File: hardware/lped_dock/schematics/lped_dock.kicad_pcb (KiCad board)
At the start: 2 copper layers, 35.4 x 16 mm, 25 parts, among them J2 V_{OUT}, J3 BUTTON, J4 CONN, J5 LED, J6 GND, J7 USB-C connector, SW1 Pair button, U1 TPD4E02B04DQA, U2 TPS560200

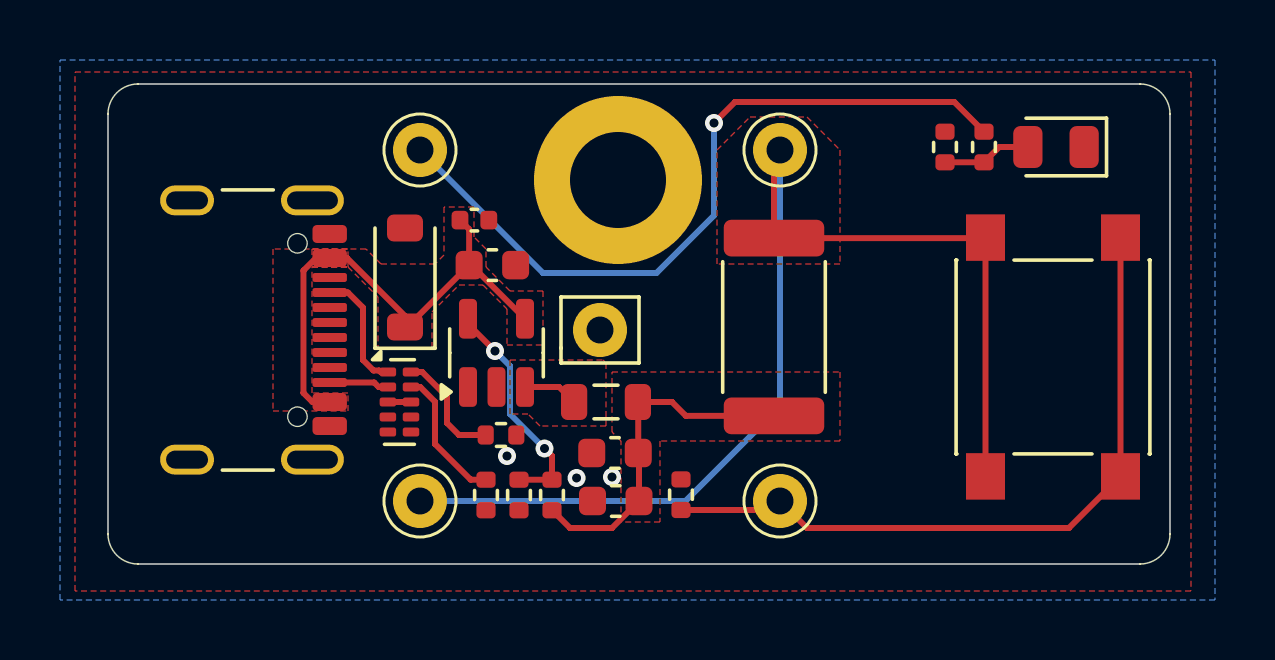
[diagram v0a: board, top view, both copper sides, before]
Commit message: feat(hardware): remove unused parts from dock pcb
* Removed LED from dock
* Removed button from dock
* Removed connection pins for LED and button
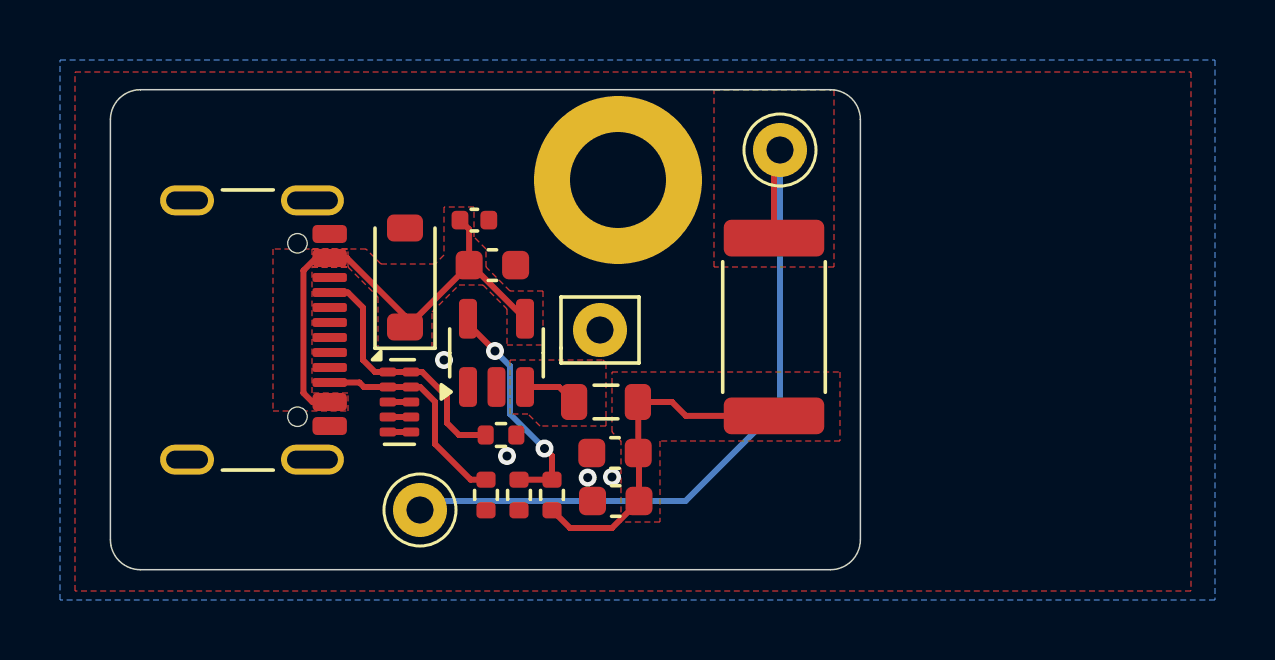
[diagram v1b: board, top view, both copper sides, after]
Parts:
- removed D1: LED, Diode_SMD:D_0805_2012Metric
- removed the J3 at (125.0, 112.7)
- removed J5: LED, Connector_Pin:Pin_D0.9mm_L10.0mm_W2.4mm_FlatFork
- removed R1: 1k, Resistor_SMD:R_0402_1005Metric
- removed R7, R8: 10k, Resistor_SMD:R_0402_1005Metric
- removed SW1: Pair button, Button_Switch_SMD:SW_SPST_PTS645
- moved J2 0.30 mm to (113.0, 113.0)
- renumbered J2 to J1, J4 to J2, J6 to J3
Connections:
- J7 pad A5: /USB/USB_CC1 -> /USB/CC1
- J7 pad B5: /USB/USB_CC2 -> /USB/CC2
- U1 pad 1: /USB/USB_CC1 -> /USB/CC1
- U1 pad 2: /USB/USB_CC2 -> /USB/CC2
- U1 pad 4: /USB/USB_D- -> /USB/D-
- U1 pad 5: /USB/USB_D+ -> /USB/D+
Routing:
- net /Dice Connector/LED: track 25.1 -> 0.00 mm, vias 1 -> 0
- net /Dice Connector/BUTTON: track 23.8 -> 0.00 mm
- net 3V6: track 39.9 -> 24.9 mm
- net /USB/CC1: track 3.87 -> 8.70 mm
- net /USB/USB_CC1: track 4.06 -> 0.00 mm
- net Net-(D1-A): track 2.97 -> 0.00 mm
- net /USB/CC2: track 4.60 -> 7.38 mm
- net /USB/USB_CC2: track 2.00 -> 0.00 mm
- net /USB/D-: track 0.00 -> 0.77 mm
- net /USB/D+: track 0.00 -> 0.77 mm
- net Earth: vias 3 -> 4
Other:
- board size 35.4 x 16 mm -> 25 x 16 mm
- board text added: "V2.0"
- board text removed: "BUTTON"
- board text removed: "LED"
- board text removed: "V1.0"

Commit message: feat(hardware): minor single dock improvements
* Moved connection pins closer together
* Added ground stiching
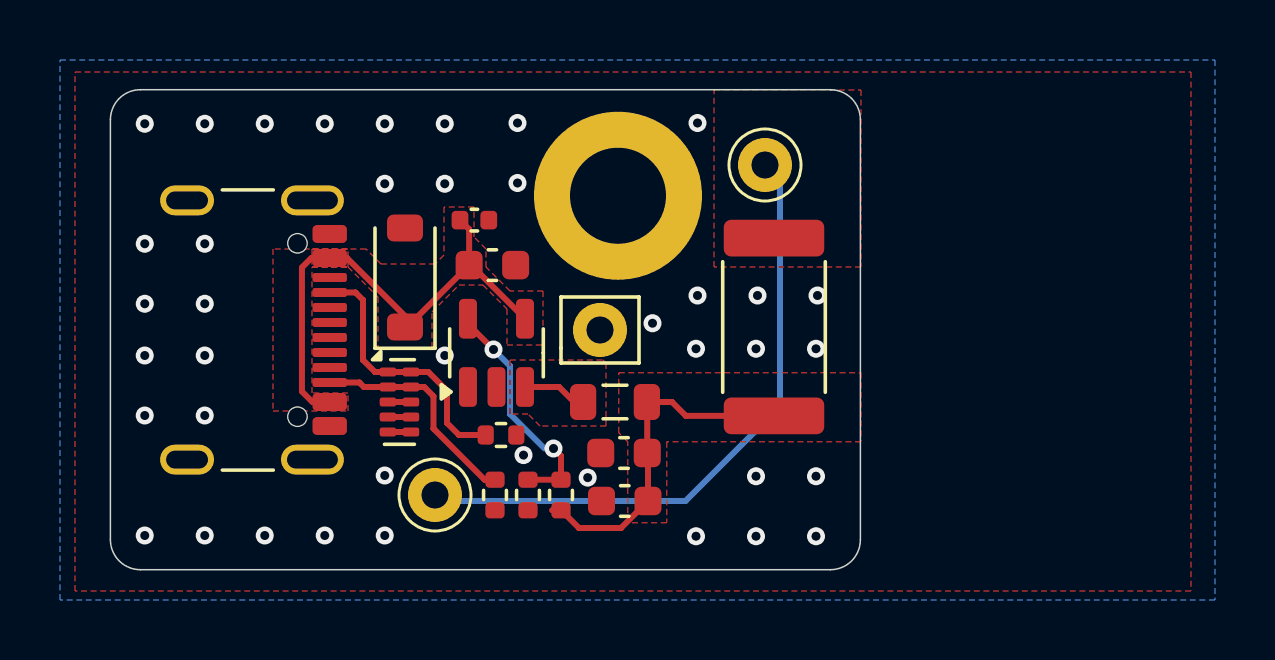
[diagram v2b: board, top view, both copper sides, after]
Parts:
- moved J1 0.71 mm to (124.5, 101.5)
- moved J2 0.71 mm to (113.5, 112.5)
- moved H1 0.53 mm to (119.6, 102.5)
- moved C1 0.30 mm to (119.8, 111.1)
- moved C2 0.30 mm to (119.8, 112.7)
- moved L1 0.30 mm to (119.5, 109.4)
- moved R3 0.30 mm to (117.7, 112.5)
- moved R4 0.30 mm to (116.6, 112.5)
- moved R6 0.30 mm to (115.5, 112.5)
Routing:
- net 3V6: track 24.9 -> 22.1 mm
- net Earth: vias 4 -> 40
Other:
- board text added: "V2.0-Single"
- board text removed: "V2.0"
